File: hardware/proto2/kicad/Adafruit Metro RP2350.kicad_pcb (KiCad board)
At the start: 4 copper layers, 41.4 x 77.8 mm, 68 parts, among them J1 USB_C_Receptacle_USB2.0_14P, J2 Conn_02x09_Counter_Clockwise, J3 Conn_01x05_Pin, U1 APS1604M-3SQRx-SN, U2 W25Q128JVS, U4 74LVC1G19, U5 NCP1117-3.3_SOT223, U7 APS1604M-3SQRx-SN, X4 RP2350B, Y1 12MHz_10pF_50ohm

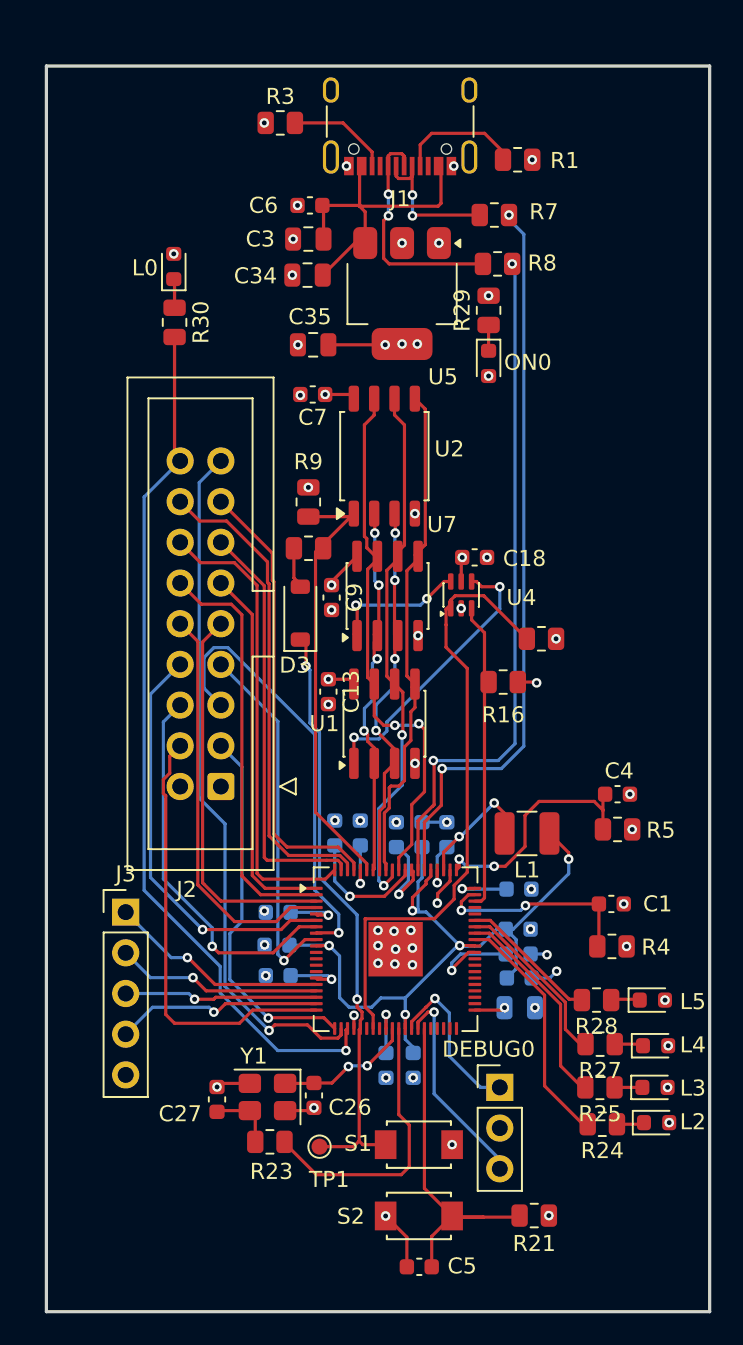
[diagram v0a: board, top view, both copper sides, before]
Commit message: proto2: smaller footprints, direct camera wiring, CAN block, 40x40 placement
- Passives moved to 0402 (10 uF to 0603), diodes to SOD-523, LEDs to 0402,
  with LCSC numbers for JLC basic/preferred parts where available
- All footprints from the standard KiCad libraries; Eagle-imported LED,
  diode, inductor and test point pins renumbered to match the pads
- Camera header pair (J2, JP1, JP2) removed and the camera wired straight
  to the RP2350B; D2-D9 now on GPIO0-7 in order; camera reset on its own
  net (GPIO22) instead of the RP2350 RUN net
- CAN: JST SH connector (J4), jumper-selectable 120 R terminator, MCP2515
  on SPI0 (GPIO32-35), INT on GPIO36, transceiver standby on GPIO37,
  16 MHz crystal
- A0 (GPIO41) no longer shorted to the MCP2515 3.3 V node
- SJ1 bridged to the RP2350 XCLK by default, OSC1 not populated
- Camera breakout power LED (D2, SJ3, R2) removed, ON0 populated
- PCB: 40 x 40 mm outline, old routing cleared, rough two-sided placement

Co-Authored-By: Claude Opus 5.5 <noreply@anthropic.com>
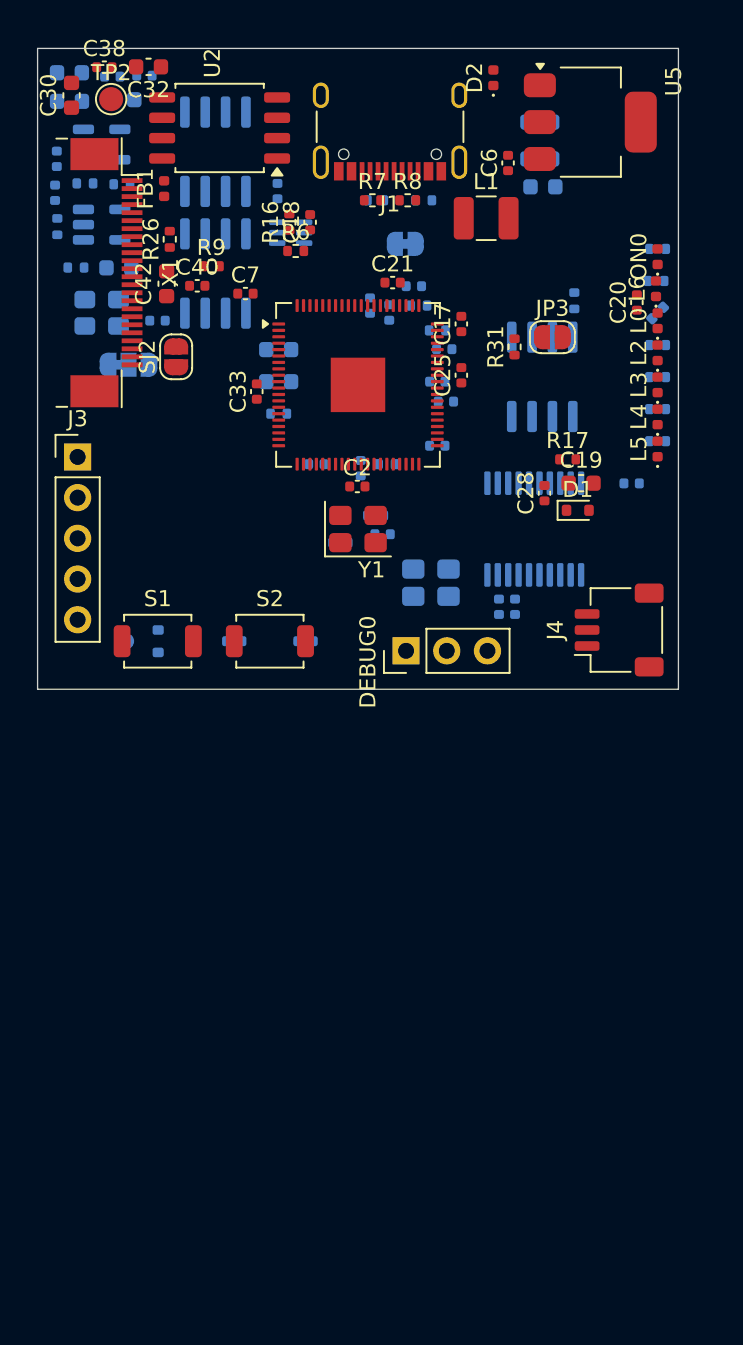
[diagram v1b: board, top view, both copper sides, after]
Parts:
- removed J2: Conn_02x09_Counter_Clockwise, Connector_IDC:IDC-Header_2x09_P2.54mm_Vertical
- added C19: 10uF, Capacitor_SMD:C_0603_1608Metric, F.Cu at (53.9, 47.1)
- added C20: 0.1uF, Capacitor_SMD:C_0402_1005Metric, F.Cu at (57.4, 35.9)
- added C28: 0.1uF, Capacitor_SMD:C_0402_1005Metric, F.Cu at (51.6, 47.8)
- added C29: 10uF, Capacitor_SMD:C_0603_1608Metric, B.Cu at (22.0, 21.5)
- added C30: 10uF, Capacitor_SMD:C_0603_1608Metric, F.Cu at (22.1, 22.9)
- added C31: 10uF, Capacitor_SMD:C_0603_1608Metric, B.Cu at (22.0, 23.3)
- added C32: 10uF, Capacitor_SMD:C_0603_1608Metric, F.Cu at (26.9, 21.1)
- added C36: 10uF, Capacitor_SMD:C_0603_1608Metric, B.Cu at (25.3, 23.2)
- added C37: 0.1uF, Capacitor_SMD:C_0402_1005Metric, B.Cu at (24.7, 21.8)
- added C38: 0.1uF, Capacitor_SMD:C_0402_1005Metric, F.Cu at (24.2, 21.2)
- added C39: 0.1uF, Capacitor_SMD:C_0402_1005Metric, B.Cu at (21.2, 26.9)
- added C40: 0.1uF, Capacitor_SMD:C_0402_1005Metric, F.Cu at (30.0, 34.8)
- added C41: 1.0uF, Capacitor_SMD:C_0402_1005Metric, B.Cu at (21.1, 29.0)
- added C42: 10uF, Capacitor_SMD:C_0603_1608Metric, F.Cu at (28.1, 34.7)
- added C43: 10uF, Capacitor_SMD:C_0603_1608Metric, B.Cu at (25.1, 33.7)
- added C44: 22pF, Capacitor_SMD:C_0402_1005Metric, B.Cu at (27.5, 37.0)
- added C45: 100n, Capacitor_SMD:C_0402_1005Metric, B.Cu at (57.1, 47.1)
- added C46: 12pF, Capacitor_SMD:C_0402_1005Metric, B.Cu at (48.8, 54.9)
- added C47: 12pF, Capacitor_SMD:C_0402_1005Metric, B.Cu at (49.8, 54.9)
- added D1: 1N4148WT, Diode_SMD:D_SOD-523, F.Cu at (53.7, 48.8)
- added D2: GREEN, LED_SMD:LED_0402_1005Metric, F.Cu at (48.5, 21.8)
- added FB1: ferrite, Inductor_SMD:L_0402_1005Metric, F.Cu at (27.9, 28.8)
- added J4: CAN, Connector_JST:JST_SH_SM03B-SRSS-TB_1x03-1MP_P1.00mm_Horizontal, F.Cu at (56.3, 56.3)
- added JP3: CAN_TERM, Jumper:SolderJumper-2_P1.3mm_Open_RoundedPad1.0x1.5mm, F.Cu at (52.1, 38.0)
- added L6: RED, LED_SMD:LED_0402_1005Metric, F.Cu at (58.6, 35.0)
- added OSC1: 24MHz 3.3V Oscillator, Oscillator:Oscillator_SMD_Abracon_ASE-4Pin_3.2x2.5mm, B.Cu at (24.0, 36.5)
- added R10: 10K, Resistor_SMD:R_0402_1005Metric, B.Cu at (23.0, 28.4)
- added R11: 10K, Resistor_SMD:R_0402_1005Metric, B.Cu at (22.4, 33.7)
- added R12: 10K, Resistor_SMD:R_0402_1005Metric, B.Cu at (25.3, 28.5)
- added R13: 10K, Resistor_SMD:R_0402_1005Metric, B.Cu at (21.2, 31.1)
- added R15: 2.2K, Resistor_SMD:R_0402_1005Metric, B.Cu at (58.6, 34.5)
- added R17: 10K, Resistor_SMD:R_0402_1005Metric, F.Cu at (53.1, 45.6)
- added R2: 10K, Resistor_SMD:R_0402_1005Metric, B.Cu at (35.0, 42.8)
- added R31: 120, Resistor_SMD:R_0402_1005Metric, F.Cu at (49.8, 38.6)
- added R32: 10K, Resistor_SMD:R_0402_1005Metric, B.Cu at (53.5, 35.8)
- added SJ1: SOLDERJUMPER_2WAY, Jumper:SolderJumper-3_P1.3mm_Bridged12_RoundedPad1.0x1.5mm_NumberLabels, B.Cu at (25.7, 39.7)
- added SJ2: SOLDERJUMPER, Jumper:SolderJumper-2_P1.3mm_Open_RoundedPad1.0x1.5mm, F.Cu at (28.6, 39.2)
- added SJ3: SOLDERJUMPERCLOSED, Jumper:SolderJumper-2_P1.3mm_Bridged_RoundedPad1.0x1.5mm, B.Cu at (43.0, 32.2)
- added TP2: TESTPOINTROUND1.5MM, TestPoint:TestPoint_Pad_D1.5mm, F.Cu at (24.6, 23.2)
- added U3: MCP2515-xST, Package_SO:TSSOP-20_4.4x6.5mm_P0.65mm, B.Cu at (51.0, 50.0)
- added U6: SN65HVD230, Package_SO:SOIC-8_3.9x4.9mm_P1.27mm, B.Cu at (51.5, 40.5)
- added U8: TLV74328, Package_TO_SOT_SMD:SOT-23-5, B.Cu at (24.0, 26.0)
- added U9: TLV74315, Package_TO_SOT_SMD:SOT-23-5, B.Cu at (24.0, 31.0)
- added X1: CAMERA_OV2640, Connector_FFC-FPC:Jushuo_AFC07-S24FCA-00_1x24-1MP_P0.50_Horizontal, F.Cu at (24.3, 34.0)
- added Y2: 16MHz, Crystal:Crystal_SMD_3225-4Pin_3.2x2.5mm, B.Cu at (44.5, 53.4)
- C1, C13, C26, C27, C4, C5, C9: footprint Capacitor_SMD:C_0603_1608Metric -> Capacitor_SMD:C_0402_1005Metric; moved to B.Cu
- C10: footprint Capacitor_SMD:C_0805_2012Metric -> Capacitor_SMD:C_0603_1608Metric
- C11, C12, C14, C16, C18, C22, C23, C24, C6, C7, C8: footprint Capacitor_SMD:C_0603_1608Metric -> Capacitor_SMD:C_0402_1005Metric
- C17, C2, C21, C25, C33: footprint Capacitor_SMD:C_0603_1608Metric -> Capacitor_SMD:C_0402_1005Metric; moved to F.Cu
- C3, C34, C35: footprint Capacitor_SMD:C_0805_2012Metric -> Capacitor_SMD:C_0603_1608Metric; moved to B.Cu
- D3: footprint Diode_SMD:D_SOD-123 -> Diode_SMD:D_SOD-523; moved to B.Cu
- L0, L2, L3, L4, L5, ON0: footprint LED_SMD:LED_0603_1608Metric -> LED_SMD:LED_0402_1005Metric
- R1, R21, R23, R24, R25, R27, R28, R29, R3, R30, R4, R5: footprint Resistor_SMD:R_0805_2012Metric -> Resistor_SMD:R_0402_1005Metric; moved to B.Cu
- R16, R26, R6, R7, R8, R9: footprint Resistor_SMD:R_0805_2012Metric -> Resistor_SMD:R_0402_1005Metric
- S1, S2: footprint lib_foot:SW_TS-1088-AR02016 -> Button_Switch_SMD:SW_SPST_TS-1088-xR020
- TP1, U1, U4, U7: moved to B.Cu
- moved R24 48.8 mm to (58.7, 38.5)
- moved L2 48.1 mm to (58.7, 39.0), turned to 90 degrees
- moved R21 47.8 mm to (41.8, 46.0), turned to 0 degrees
- moved R25 44.5 mm to (58.7, 40.5)
- moved L3 43.9 mm to (58.7, 41.0), turned to 90 degrees
- moved C10 43.7 mm to (35.0, 38.8)
- moved C23 42.2 mm to (40.8, 36.0), turned to 90 degrees
- moved C15 40.1 mm to (35.0, 40.8), turned to 0 degrees
- moved C13 40.1 mm to (26.7, 21.7), turned to 0 degrees
- moved C8 40.1 mm to (42.0, 36.5), turned to 90 degrees
- moved R4 40.0 mm to (45.0, 37.6)
- moved R27 39.8 mm to (58.7, 42.5)
- moved C5 39.7 mm to (36.7, 57.0)
- moved R23 39.7 mm to (41.1, 49.1)
- moved L4 39.3 mm to (58.7, 43.0), turned to 90 degrees
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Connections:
- net /PD renamed PWDN
- net ~{RESET} renamed /~{RESET}
- R24 pad 1: Net-(L2-PadA) -> Net-(L2-A)
- R24 pad 2: 3.3V -> /A0
- R25 pad 1: Net-(L3-PadA) -> Net-(L3-A)
- R26 pad 2: Net-(D3-PadA) -> Net-(D3-A)
- R27 pad 1: Net-(L4-PadA) -> Net-(L4-A)
- R28 pad 1: Net-(L5-PadA) -> Net-(L5-A)
- R29 pad 1: Net-(ON0-PadA) -> Net-(ON0-A)
- R30 pad 1: Net-(L0-PadA) -> Net-(L0-A)
- X4 pad 1: /D7 -> DATA6
- X4 pad 2: /D6 -> DATA7
- X4 pad 22: /RT -> CAM_~{RESET}
- X4 pad 3: /D9 -> DATA8
- X4 pad 4: /D8 -> DATA9
- X4 pad 40: unconnected-(X4-GPIO32/MISO0/TX0/SDA0/PWM8A-Pad40) -> /CAN_MISO
- X4 pad 42: unconnected-(X4-GPIO33/CS0/RX0/SCL0/PWM8B-Pad42) -> /CAN_CS
- X4 pad 43: unconnected-(X4-GPIO34/SCK0/CTS0/SDA1/PWM9A-Pad43) -> /CAN_SCK
- X4 pad 44: unconnected-(X4-GPIO35/MOSI0/RTS0/SCL1/PWM9B-Pad44) -> /CAN_MOSI
- X4 pad 45: unconnected-(X4-GPIO36/MISO0/TX1/SDA0/PWM10A-Pad45) -> /CAN_INT
- X4 pad 46: unconnected-(X4-GPIO37/CS0/RX1/SCL0/PWM10B-Pad46) -> /CAN_STBY
- X4 pad 52: 3.3V -> /A0
- X4 pad 6: /XC -> EXT_XCLK
- X4 pad 7: /HS -> HSYNC
- X4 pad 77: /D3 -> DATA2
- X4 pad 78: /D2 -> DATA3
- X4 pad 79: /D5 -> DATA4
- X4 pad 8: /VS -> VSYNC
- X4 pad 80: /D4 -> DATA5
- X4 pad 9: /PC -> PCLK
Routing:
- net 3.3V: track 71.1 -> 0.00 mm, vias 26 -> 0
- net PWDN: track 54.7 -> 0.00 mm, vias 1 -> 0
- net 1.2V: track 48.2 -> 0.00 mm, vias 5 -> 0
- net /D-: track 46.0 -> 0.00 mm, vias 2 -> 0
- net /RT: track 43.4 -> 0.00 mm, vias 1 -> 0
- net /D+: track 42.8 -> 0.00 mm, vias 2 -> 0
- net /GPIO26: track 38.9 -> 0.00 mm
- net /USBBOOT: track 37.3 -> 0.00 mm, vias 2 -> 0
- net /QSPI_DATA[3]: track 33.2 -> 0.00 mm, vias 2 -> 0
- net /QSPI_SCK: track 33.0 -> 0.00 mm, vias 2 -> 0
- net /QSPI_DATA[0]: track 31.3 -> 0.00 mm
- net /D2: track 30.2 -> 0.00 mm
- net /D4: track 29.1 -> 0.00 mm
- net /D3: track 28.3 -> 0.00 mm
- net /QSPI_CS: track 27.5 -> 0.00 mm
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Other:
- board size 41.4 x 77.8 mm -> 40 x 40 mm

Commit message: Show proto2 in the main README, add proto2 renders
- Main README: proto2 renders instead of proto1, "proto2 at a glance"
  with the block diagram extended by the CAN bus and camera regulators
- proto1 README now shows its own renders
- proto2 docs/: schematic PDF and top/bottom renders of the placement
- export-docs.sh renders proto2 square (40 x 40 mm board)
- PCB synced with the schematic: D2, SJ3, R2 removed, ON0 populated

Co-Authored-By: Claude Opus 5.5 <noreply@anthropic.com>
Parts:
- removed D2: GREEN, LED_SMD:LED_0402_1005Metric
- removed R2: 10K, Resistor_SMD:R_0402_1005Metric
- removed SJ3: SOLDERJUMPERCLOSED, Jumper:SolderJumper-2_P1.3mm_Bridged_RoundedPad1.0x1.5mm
